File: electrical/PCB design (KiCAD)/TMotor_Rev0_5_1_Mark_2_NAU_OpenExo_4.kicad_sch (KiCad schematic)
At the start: 4 parts

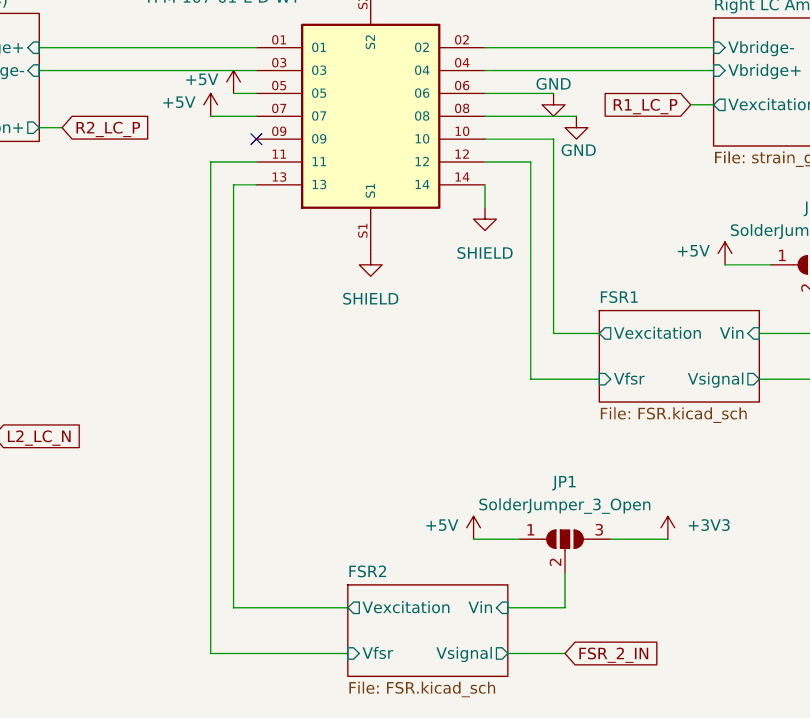
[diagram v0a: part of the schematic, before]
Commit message: fixed singleLeg python scripts
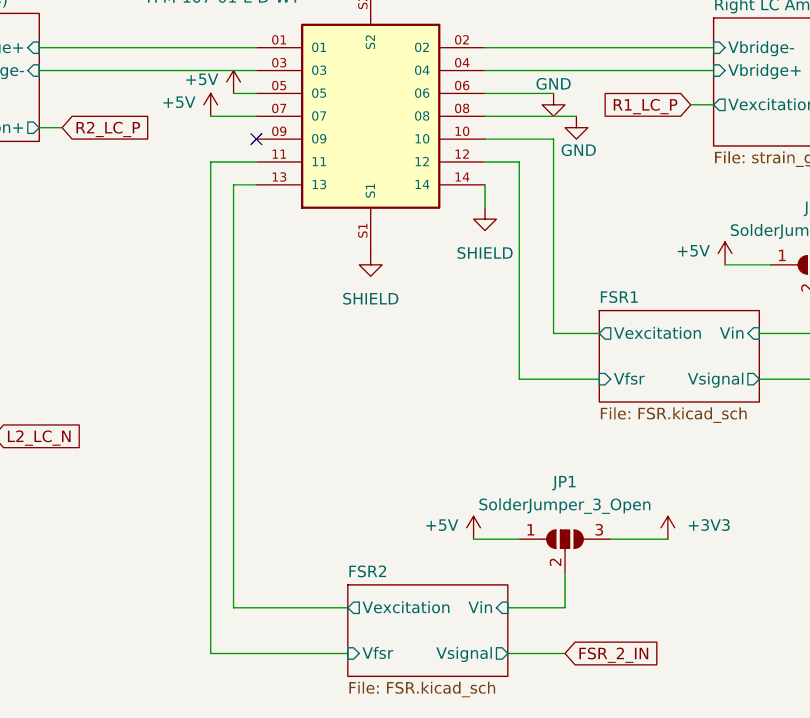
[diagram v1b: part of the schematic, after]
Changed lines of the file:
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@@
+	(wire
+		(pts
+			(xy 248.92 101.6) (xy 248.92 125.73)
+		)
+		(stroke
+			(width 0)
+			(type default)
+		)
+	)
 	(wire
 		(pts
@@
 	(wire
 		(pts
-			(xy 214.63 101.6) (xy 214.63 156.21)
-		)
-		(stroke
-			(width 0)
-			(type default)
-		)
-	)
-	(wire
-		(pts
 			(xy 125.73 128.27) (xy 160.02 128.27)
 		)
@@
 	(wire
 		(pts
-			(xy 219.71 101.6) (xy 214.63 101.6)
-		)
-		(stroke
-			(width 0)
-			(type default)
-		)
-	)
-	(wire
-		(pts
 			(xy 217.17 151.13) (xy 229.87 151.13)
 		)
@@
 	(wire
 		(pts
-			(xy 245.11 101.6) (xy 250.19 101.6)
+			(xy 214.63 101.6) (xy 219.71 101.6)
 		)
 		(stroke
@@
 	(wire
 		(pts
-			(xy 250.19 125.73) (xy 257.81 125.73)
-		)
-		(stroke
-			(width 0)
-			(type default)
-		)
-	)
-	(wire
-		(pts
 			(xy 232.41 77.47) (xy 237.49 77.47)
 		)
@@
 	(wire
 		(pts
+			(xy 245.11 101.6) (xy 248.92 101.6)
+		)
+		(stroke
+			(width 0)
+			(type default)
+		)
+	)
+	(wire
+		(pts
 			(xy 245.11 104.14) (xy 245.11 106.68)
 		)
@@
 	(wire
 		(pts
+			(xy 214.63 156.21) (xy 214.63 101.6)
+		)
+		(stroke
+			(width 0)
+			(type default)
+		)
+	)
+	(wire
+		(pts
 			(xy 232.41 81.28) (xy 232.41 77.47)
 		)
@@
 	(wire
 		(pts
+			(xy 248.92 125.73) (xy 257.81 125.73)
+		)
+		(stroke
+			(width 0)
+			(type default)
+		)
+	)
+	(wire
+		(pts
 			(xy 245.11 88.9) (xy 270.51 88.9)
 		)
@@
 	(wire
 		(pts
+			(xy 163.83 90.17) (xy 166.37 90.17)
+		)
+		(stroke
+			(width 0)
+			(type default)
+		)
+	)
+	(wire
+		(pts
+			(xy 217.17 104.14) (xy 217.17 151.13)
+		)
+		(stroke
+			(width 0)
+			(type default)
+		)
+	)
+	(wire
+		(pts
+			(xy 125.73 130.81) (xy 160.02 130.81)
+		)
+		(stroke
+			(width 0)
+			(type default)
+		)
+	)
+	(wire
+		(pts
+			(xy 195.58 91.44) (xy 219.71 91.44)
+		)
+		(stroke
+			(width 0)
+			(type default)
+		)
+	)
+	(wire
+		(pts
 			(xy 214.63 156.21) (xy 229.87 156.21)
 		)
 		(stroke
-			(width 0)
-			(type default)
-		)
-	)
-	(wire
-		(pts
-			(xy 250.19 101.6) (xy 250.19 125.73)
-		)
-		(stroke
-			(width 0)
-			(type default)
-		)
-	)
-	(wire
-		(pts
-			(xy 163.83 90.17) (xy 166.37 90.17)
-		)
-		(stroke
-			(width 0)
-			(type default)
-		)
-	)
-	(wire
-		(pts
-			(xy 217.17 104.14) (xy 217.17 151.13)
-		)
-		(stroke
-			(width 0)
-			(type default)
-		)
-	)
-	(wire
-		(pts
-			(xy 125.73 130.81) (xy 160.02 130.81)
-		)
-		(stroke
-			(width 0)
-			(type default)
-		)
-	)
-	(wire
-		(pts
-			(xy 195.58 91.44) (xy 219.71 91.44)
-		)
-		(stroke
